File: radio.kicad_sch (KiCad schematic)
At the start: 17 parts, among them U18 RP2350B, U19 ABM8-272-T3_C20625731, U20 CC1101RGPR, U21 PE4259-63, U22 PN7150B0HN/C11002Y, U23 EM4095HMSO16B+, Y1 Crystal, Y3 Crystal

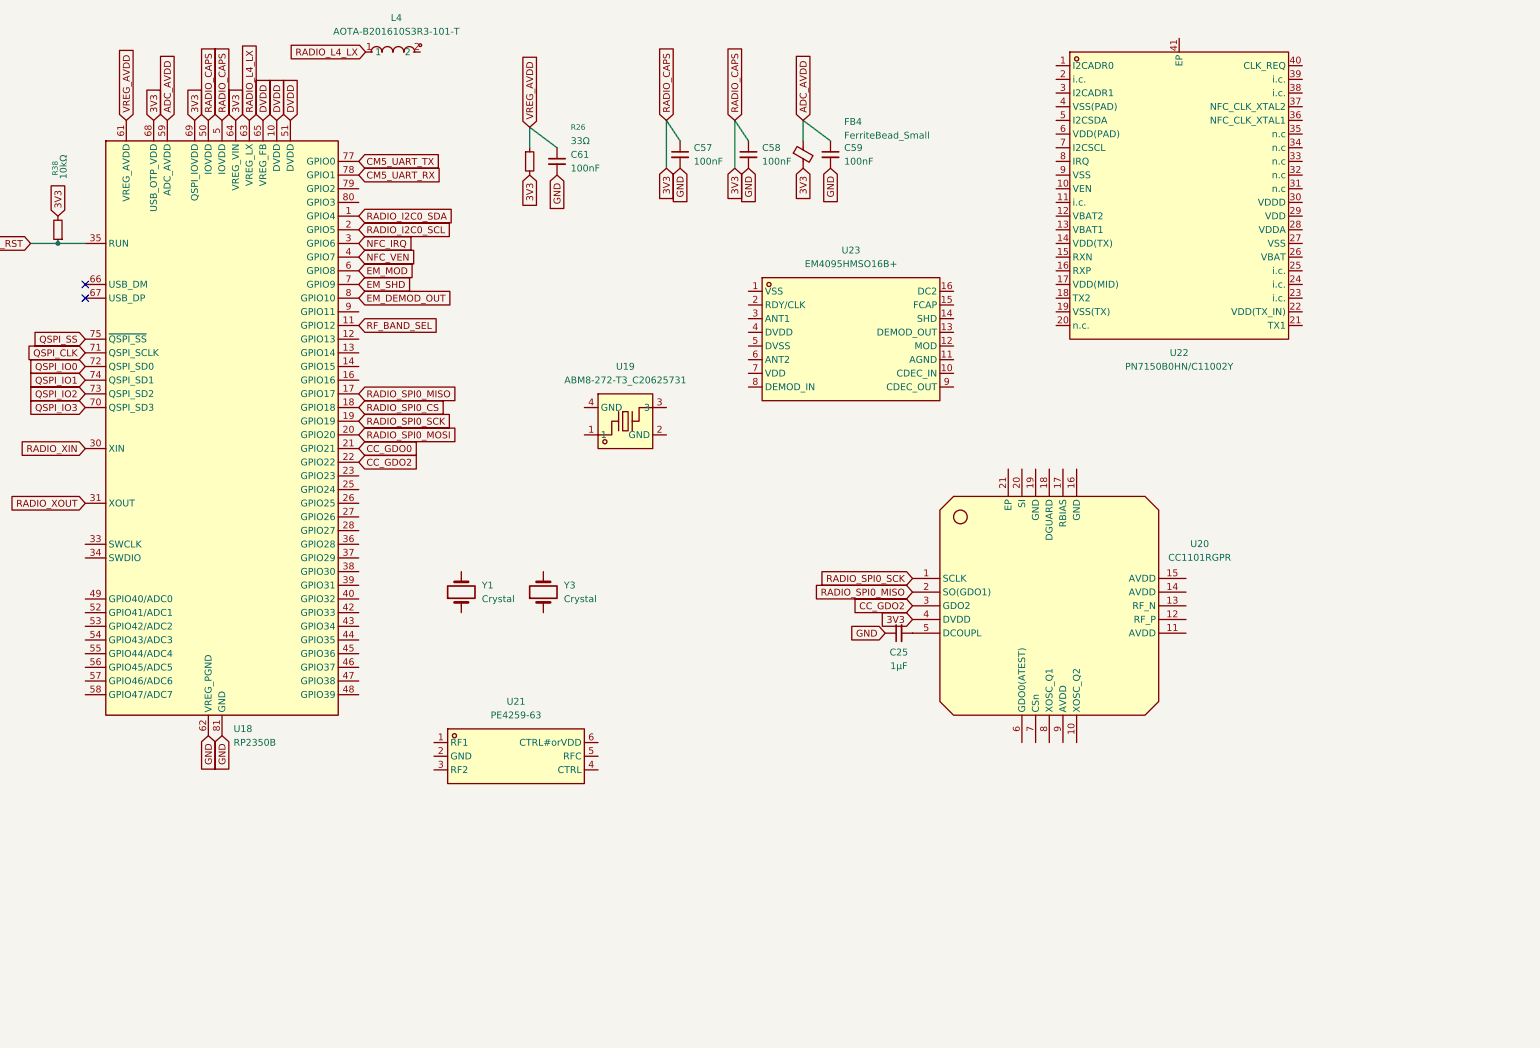
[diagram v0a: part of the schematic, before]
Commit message: finished cc1101 wiring, switched to single balun approach for dual sub-ghz bands, added sma port and footprints
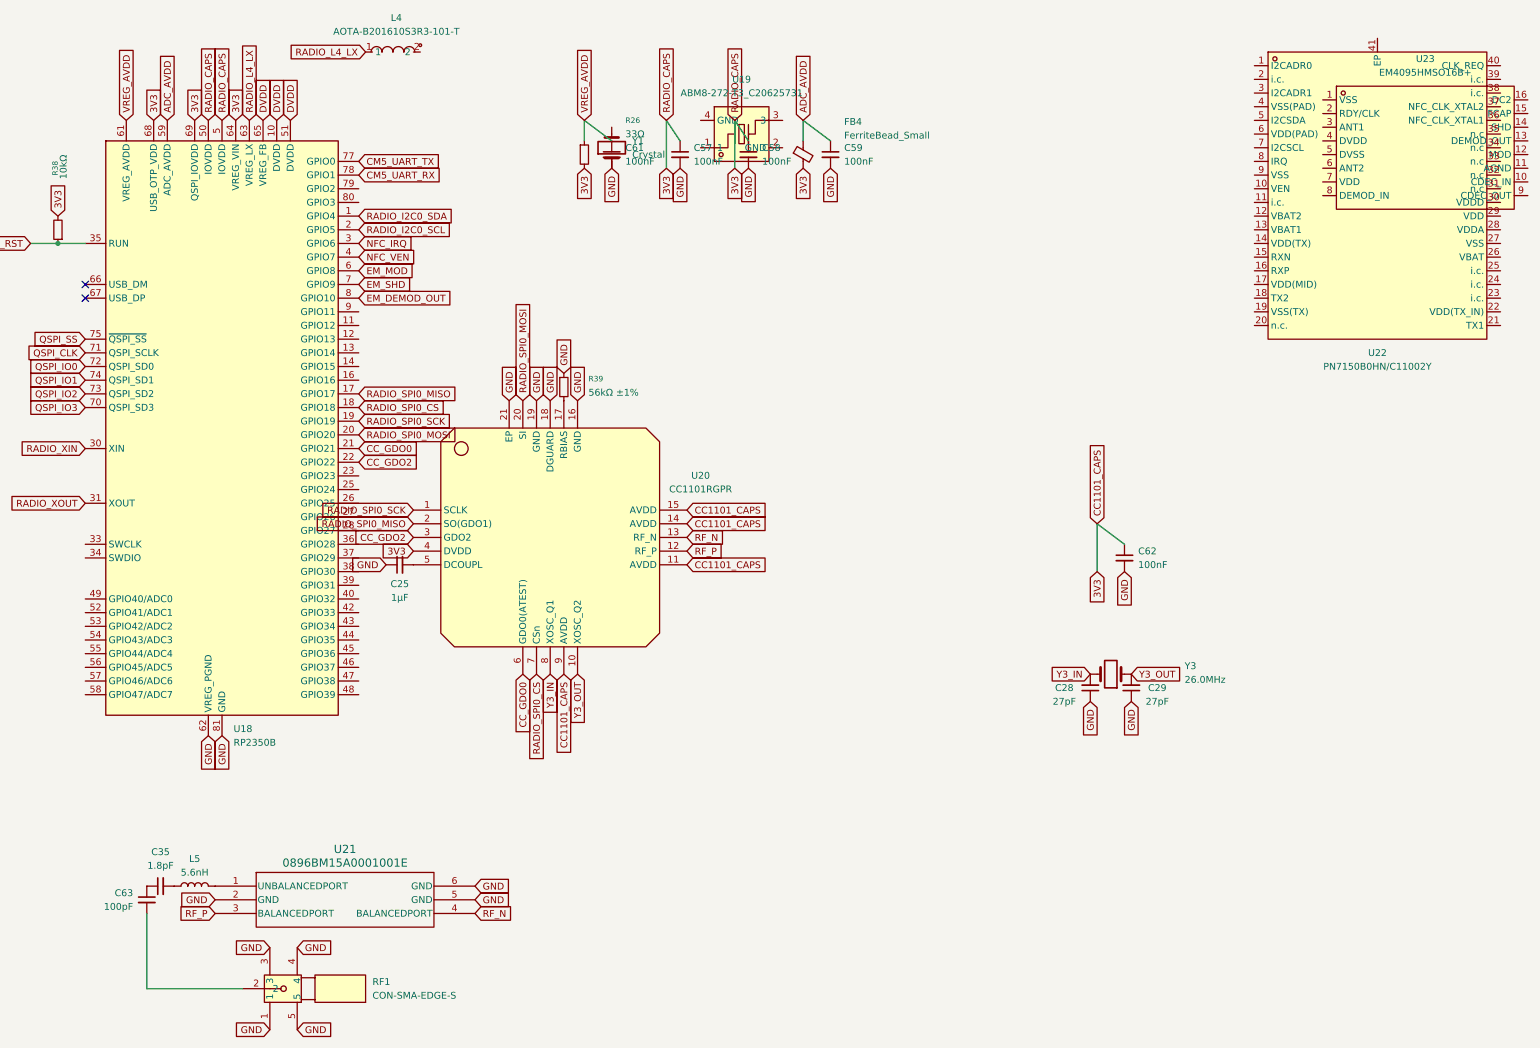
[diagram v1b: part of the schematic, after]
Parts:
- removed U21: PE4259-63, slate113:SC-70-6_L2.2-W1.3-P0.65-LS2.1-BL, symbol slate113:PE4259-63
- added C28, C29: 27pF, symbol Device:C_Small
- added C35: 1.8pF, symbol Device:C_Small
- added C62: 100nF, symbol Device:C_Small
- added C63: 100pF, symbol Device:C_Small
- added L5: 5.6nH, symbol Device:L
- added R39: 56kΩ ±1%, symbol Device:R_Small
- added RF1: CON-SMA-EDGE-S, slate113:SMA-SMD_CON-SMA-EDGE-S, symbol slate113:CON-SMA-EDGE-S
- added U21: 0896BM15A0001001E, slate113:SMD6_0896BM15A0001001E_JOT, symbol slate113:0896BM15A0001001E
- Y3: value Crystal -> 26.0MHz
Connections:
- net 3V3: now also U20.11 (AVDD), U20.14 (AVDD), U20.15 (AVDD), U20.9 (AVDD), C62.1
- net CC_GDO0: now also U20.6 (GDO0(ATEST))
- net GND: now also U20.16 (GND), U20.18 (DGUARD), U20.19 (GND), U20.21 (EP), Y1.1, C28.1, C29.1, C62.2, R39.1, RF1.1, RF1.3, RF1.4, RF1.5, U21.2 (GND), U21.5 (GND), U21.6 (GND)
- net RADIO_SPI0_CS: now also U20.7 (CSn)
- net RADIO_SPI0_MOSI: now also U20.20 (SI)
- net Y3_OUT: now reaches Y3.1
- net Y3_OUT: now also U20.10 (XOSC_Q2), C29.2
- net Y3_IN: now reaches Y3.2
- net Y3_IN: now also U20.8 (XOSC_Q1), C28.2
- net RF_P: now reaches U20.12 (RF_P)
- net RF_P: now also U21.3 (BALANCEDPORT)
- net RF_N: now reaches U20.13 (RF_N)
- net RF_N: now also U21.4 (BALANCEDPORT)
- net at U20.17 (RBIAS): now also R39.2
- net RF_BAND_SEL: no longer names the net of U18.11 (GPIO12)
- new net: C35.1, C63.1
- new net: C35.2, L5.1
- new net: C63.2, RF1.2
- new net: L5.2, U21.1 (UNBALANCEDPORT)
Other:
- moved on the sheet: C25, C61, R26, U19, U20, U22, U23, Y1, Y3

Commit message: worked on sub-ghz band switching with dual baluns and lc tuning, added second usb-c port, started nfc wiring, added switch footprint
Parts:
- added C60: 1.8pF, symbol Device:C_Small
- added C64, C65: 6.8pF, symbol Device:C_Small
- added C66: 20pF, symbol Device:C_Small
- added C67, C69, C70, C71: 100nF, symbol Device:C_Small
- added C68: 4.7µF, symbol Device:C_Small
- added FB5: FerriteBead, symbol Device:FerriteBead
- added L6, L7: 33nH, symbol Device:L
- added R40, R41: 5.1kΩ, symbol Device:R_Small
- added SW3: 4*4*1.7, slate113:SW-SMD_4P-L5.2-W5.2-P3.70-LS6.5, symbol slate113:4*4*1.7
- added U24, U25, U26, U27: PE4259-63, slate113:SC-70-6_L2.2-W1.3-P0.65-LS2.1-BL, symbol slate113:PE4259-63
- added U28: 0433BM15A0001001E, slate113:SMD6_0896BM15A0001001E_JOT, symbol slate113:0896BM15A0001001E
- added USB2: TYPE-C16PIN, slate113:USB-C-SMD_TYPE-C16PIN, symbol slate113:TYPE-C16PIN
- C35: value 1.8pF -> 20pF
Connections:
- net 3V3: now also U22.12 (VBAT2), U22.13 (VBAT1), U22.26 (VBAT), U22.6 (VDD(PAD)), C67.2, C68.1, C70.2, C71.2, U24.6 (CTRL#orVDD), U25.6 (CTRL#orVDD), U26.6 (CTRL#orVDD), U27.6 (CTRL#orVDD)
- net GND: now also C35.1, U19.2 (GND), U19.4 (GND), U22.1 (I2CADR0), U22.14 (VDD(TX)), U22.17 (VDD(MID)), U22.19 (VSS(TX)), U22.22 (VDD(TX_IN)), U22.27 (VSS), U22.28 (VDDA), U22.29 (VDD), U22.3 (I2CADR1), U22.30 (VDDD), U22.4 (VSS(PAD)), U22.41 (EP), U22.9 (VSS), C66.2, C67.1, C69.2, C70.1, C71.1, FB5.2, L6.2, L7.2, R40.2, R41.2, SW3.3, SW3.4, U24.2 (GND), U25.2 (GND), U26.2 (GND), U27.2 (GND), U28.2 (GND), U28.5 (GND), U28.6 (GND), USB2.A1B12 (GND), USB2.B1A12 (GND); no longer C61.2
- net NFC_IRQ: now also U22.8 (IRQ)
- net NFC_VEN: now also U22.10 (VEN)
- net QSPI_SS: now also SW3.1, SW3.2
- net RADIO_I2C0_SCL: now also U22.7 (I2CSCL)
- net RADIO_I2C0_SDA: now also U22.5 (I2CSDA)
- net RF_N: now also U27.5 (RFC); no longer U21.4 (BALANCEDPORT)
- net RF_P: now also U26.5 (RFC); no longer U21.3 (BALANCEDPORT)
- net 315MHZ_OUT: now reaches C63.1
- net 315MHZ_OUT: now also RF1.2, C65.2, U28.1 (UNBALANCEDPORT); no longer C35.1
- net at L5.1: now also C60.2; no longer C35.2
- net NFC_RX_N: now reaches U22.15 (RXN)
- net NFC_RX_P: now reaches U22.16 (RXP)
- net NFC_TX2: now reaches U22.18 (TX2)
- net NFC_TX1: now reaches U22.21 (TX1)
- net NFC_XTAL1: now reaches U22.36 (NFC_CLK_XTAL1)
- net NFC_XTAL1: now also U19.1, C66.1
- net NFC_XTAL2: now reaches U22.37 (NFC_CLK_XTAL2)
- net NFC_XTAL2: now also C35.2, U19.3
- net at Y1.2: now also C61.2
- net at C63.2: now also C60.1; no longer RF1.2
- net BAND_SEL_1: now reaches U18.11 (GPIO12)
- net BAND_SEL_1: now also U26.4 (CTRL), U27.4 (CTRL)
- net BAND_SEL_2: now reaches U18.12 (GPIO13)
- net BAND_SEL_2: now also U24.4 (CTRL), U25.4 (CTRL)
- new net: R40.1, USB2.A5 (CC1)
- new net: U25.5 (RFC), U27.3 (RF2)
- new net: R41.1, USB2.B5 (CC2)
- new net: U21.3 (BALANCEDPORT), U26.1 (RF1)
- new net: U24.5 (RFC), U26.3 (RF2)
- new net: C68.2, C69.1
- new net BADUSB_DM: USB2.A7 (DN1), USB2.B7 (DN2)
- new net BADUSB_DP: USB2.A6 (DP1), USB2.B6 (DP2)
- new net FerriteGND_RADIO: FB5.1, USB2.1 (SHELL), USB2.2 (SHELL), USB2.3 (SHELL), USB2.4 (SHELL)
- new net U21_BPN: U21.4 (BALANCEDPORT), U27.1 (RF1)
- new net U24_RF1: C64.1, C65.1, L7.1, U24.1 (RF1)
- new net U25_RF1: C64.2, L6.1, U25.1 (RF1)
- new net U28_BPN: U25.3 (RF2), U28.4 (BALANCEDPORT)
- new net U28_BPP: U24.3 (RF2), U28.3 (BALANCEDPORT)
- no-connect marks 2 -> 20
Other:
- note added: "3-Way SMA"
- note added: "315MHz Makeshift Balun"
- note added: "BOOTSEL Button"
- note added: "BadUSB Port"
- note added: "Band Filter"
- note added: "CC1101"
- note added: "Decoupling"
- note added: "Decoupling - 3V3"
- note added: "Misc"
- note added: "NFC"
- note added: "RP2350B"
- moved on the sheet: C25, C28, C29, C57, C58, C59, C61, C62, FB4, L4, R26, R38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

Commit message: switched nfc ic, wired rfid ic, blocked on coil parameters for radio schematic
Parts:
- removed U22: PN7150B0HN/C11002Y, slate113:VQFN-40_L6.0-W6.0-P0.50-TL-EP4.5, symbol slate113:PN7150B0HN_C11002Y
- added C72, C74, C75, C79: 2.2µF, symbol Device:C_Small
- added C73, C77: 100nF, symbol Device:C_Small
- added C76: 1µF, symbol Device:C_Small
- added C78: 160nF, symbol Device:C_Small
- added C80: 10nF, symbol Device:C_Small
- added C81: 6.8nF, symbol Device:C_Small
- added C82, C83, C84, C85: 4.7uF, symbol Device:C_Small
- added U29: PN7160A1HN/C100Y, slate113:HVQFN-40_L6.0-W6.0-P0.50-BL-EP4.1, symbol slate113:PN7160A1HN_C100Y
- C71: value 100nF -> 4.7µF
- U19: value ABM8-272-T3_C20625731 -> TXM27.12M0004322DBBDO00T
- Y1: value Crystal -> 12MHz
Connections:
- net 3V3: no longer C67.2, C68.1, C70.2, C71.2
- net BADUSB_DM: now also U18.66 (USB_DM)
- net BADUSB_DP: now also U18.67 (USB_DP)
- net DVDD: now also L4.2, C82.1, C83.1, C84.1, C85.1
- net EM_DEMOD_OUT: now also U23.13 (DEMOD_OUT)
- net EM_MOD: now also U23.12 (MOD)
- net EM_SHD: now also U23.14 (SHD)
- net GND: now also C68.1, C69.1, U23.1 (VSS), U23.5 (DVSS), C72.1, C73.1, C74.1, C75.1, C76.1, C78.1, C79.1, C80.1, C81.1, C82.2, C83.2, C84.2, C85.2, U29.1 (I2C_ADR0/SPI_NSS), U29.2 (DWL_REQ), U29.20 (VSS(TX)), U29.3 (l2C_ADR1/SPI_MOSI), U29.4 (Vss(PAD)), U29.41 (VSS), U29.9 (Vss(A)); no longer C67.1, C69.2, C70.1
- net NFC_IRQ: now also U29.8 (IRQ)
- net NFC_RX_N: now also U29.15 (RXN)
- net NFC_RX_P: now also U29.16 (RXP)
- net NFC_TX1: now also U29.21 (TX1)
- net NFC_TX2: now also U29.19 (TX2)
- net NFC_VEN: now also U29.10 (VEN)
- net NFC_XTAL1: now also U29.29 (XTAL2)
- net NFC_XTAL2: now also U29.30 (NFC_CLK_XTAL1)
- net RADIO_I2C0_SCL: now also U29.7 (I2C_SCL/SPI_SCK)
- net RADIO_I2C0_SDA: now also U29.5 (I2C_SDA/SPI_MISO)
- net NFC_VBAT: now reaches C68.2
- net NFC_VBAT: now also C69.2, C71.2, U29.12 (VBAT2), U29.13 (VDD(UP)), U29.28 (VBAT); no longer C69.1
- net at U23.10 (CDEC_IN): now also C77.2
- net at U23.11 (AGND): now also C78.2
- net at U23.15 (FCAP): now also C80.2
- net at U23.16 (DC2): now also C81.2
- net EM_RDY_CLK: now reaches U23.2 (RDY/CLK)
- net EM_RDY_CLK: now also U18.13 (GPIO14)
- net at U23.4 (DVDD): now also C67.2
- net at U23.7 (VDD): now also C70.2
- net at U23.9 (CDEC_OUT): now also C77.1
- new net 5V: C67.1, C70.1
- new net NFC_VDDCORE: C75.2, C79.2, U29.26 (VDD(A)), U29.27 (VDD), U29.31 (VDD(D))
- new net NFC_VDDPAD: C76.2, U29.6 (VDD(PAD))
- new net NFC_VDDTX: C72.2, C74.2, U29.14 (VDD(TX)), U29.18 (TVDD_IN), U29.22 (VDD_IN2)
- new net NFC_VMID: C73.2, U29.17 (VDD(VMID))
- no-connect marks 20 -> 17
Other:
- note added: "RFID"
- note removed: "Decoupling - 3V3"
- moved on the sheet: L4, U23

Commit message: finished gps schematic, updated footprints and 3d models
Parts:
- added C86: 100pF, symbol Device:C_Small
- added C87, C88: 33pF, symbol Device:C_Small
- added C89: 10µF, symbol Device:C_Small
- added C90, C92, C94: 100nF, symbol Device:C_Small
- added C91: 4.7µF, symbol Device:C_Small
- added C93: 2.2µF, symbol Device:C_Small
- added D2, D4: TVS, symbol Device:D
- added D3: TVS <0.6pF, symbol Device:D
- added L8: 68nH, symbol Device:L
- added Q1: NPN, symbol Simulation_SPICE:NPN
- added R42: 4.7kΩ, symbol Device:R_Small
- added R43: 10Ω, symbol Device:R_Small
- added R44: 47kΩ, symbol Device:R_Small
- added RF2: CON-SMA-EDGE-S, slate113:SMA-SMD_CON-SMA-EDGE-S, symbol slate113:CON-SMA-EDGE-S
- added U22: (no value), symbol slate113:LC29HCAMD
- added U30: SiP32508DT, Package_TO_SOT_SMD:TSOT-23-6, symbol Power_Management:SiP32508DT
- added U31, U32: S2B-PH-K-S-GW, slate113:CONN-TH_S2B-PH-K-S-GW, symbol slate113:S2B-PH-K-S-GW
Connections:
- net 3V3: now also C88.1, C91.1, C92.1, C93.1, D4.2 (A), U22.22 (V_BCKP)
- net GND: now also C87.2, C88.2, C89.2, C90.2, C91.2, C92.2, D2.1 (K), D3.1 (K), D4.1 (K), Q1.3 (E), RF2.1, RF2.3, RF2.4, RF2.5, U22.10 (GND), U22.12 (GND), U22.13 (GND), U22.24 (GND), U22.5 (D_SEL1), U22.6 (D_SEL2), U30.4 (GND)
- net RFID_ANT1: now reaches U23.3 (ANT1)
- net RFID_ANT1: now also U32.1
- net RFID_ANT2: now reaches U23.6 (ANT2)
- net RFID_ANT2: now also U32.2
- net NFC_ANT1: now reaches U29.23 (ANT1)
- net NFC_ANT1: now also U31.1
- net NFC_ANT2: now reaches U29.24 (ANT2)
- net NFC_ANT2: now also U31.2
- net GPS_1PPS: now reaches U18.14 (GPIO15)
- net GPS_1PPS: now also U22.3 (1PPS)
- net GPS_RESET: now reaches U18.16 (GPIO16)
- net GPS_RESET: now also R44.1
- net GPS_UART_TX: now reaches U18.25 (GPIO24)
- net GPS_UART_TX: now also U22.20 (TXD1/SPI_MISO)
- net GPS_UART_RX: now reaches U18.26 (GPIO25)
- net GPS_UART_RX: now also U22.21 (RXD1/SPI_MOSI)
- net GPS_EN: now reaches U18.79 (GPIO2)
- net GPS_EN: now also U30.3 (EN)
- net GPS_WI: now reaches U18.80 (GPIO3)
- net GPS_WI: now also U22.17 (WI)
- net GPS_WAKEUP: now reaches U18.9 (GPIO11)
- net GPS_WAKEUP: now also U22.1 (WAKEUP)
- new net: L8.1, R43.2
- new net: C94.2, U30.1 (OUT), U30.2 (OUT)
- new net: C93.2, U30.5 (IN), U30.6 (IN)
- new net GPS_3V3: C87.1, C89.1, C90.1, C94.1, D2.2 (A), R42.1, U22.23 (VCC)
- new net GPS_ANT: C86.1, D3.2 (A), L8.2, RF2.2
- new net GPS_RESET_N: Q1.1 (C), R42.2, U22.8 (RESET_N)
- new net GPS_RF_IN: C86.2, U22.11 (RF_IN)
- new net GPS_VDD_RF: R43.1, U22.9 (VDD_RF)
- new net NPN_B: Q1.2 (B), R44.2
- no-connect marks 17 -> 24
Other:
- note added: "Controller"
- note added: "GPS Power"

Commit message: finished radio board with load switches and flash, fixed b2b connector, started antenna module and rf sense switching circuit
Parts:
- removed C93: 2.2µF, symbol Device:C_Small
- removed C94: 100nF, symbol Device:C_Small
- removed RF1, RF2: CON-SMA-EDGE-S, slate113:SMA-SMD_CON-SMA-EDGE-S, symbol slate113:CON-SMA-EDGE-S
- removed U30: SiP32508DT, Package_TO_SOT_SMD:TSOT-23-6, symbol Power_Management:SiP32508DT
- added C95, C97: 2.2µF, symbol Device:C_Small
- added C96, C98: 100nF, symbol Device:C_Small
- added CN15: DF40C-20DP-0.4V, slate113:CONN-SMD_20P-P0.40_HRS_DF40TC-20DP-0.4V, symbol slate113:DF40C-20DP-0.4V
- added J19: SUBGHZ SMA, symbol Connector:Conn_Coaxial_Small
- added J20: GPS SMA, symbol Connector:Conn_Coaxial_Small
- added U33: W25Q128JVSIQTR, slate113:SOIC-8_L5.3-W5.3-P1.27-LS8.0-BL, symbol slate113:W25Q128JVSIQTR
- added U34, U35: SiP32508DT, Package_TO_SOT_SMD:TSOT-23-6, symbol Power_Management:SiP32508DT
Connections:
- net NFC_VBAT is gone; now on net GPS_VCC: C68.2, C69.2, C71.2, U29.12 (VBAT2), U29.13 (VDD(UP)), U29.28 (VBAT)
- net NFC_VDDPAD is gone; now on net GPS_VCC: C76.2, U29.6 (VDD(PAD))
- net 315MHZ_OUT: now also J19.1 (In)
- net 3V3: now also C95.1, CN15.7, U33.8 (VCC); no longer U20.4 (DVDD), U24.6 (CTRL#orVDD), U25.6 (CTRL#orVDD), U26.6 (CTRL#orVDD), U27.6 (CTRL#orVDD)
- net 5V: now also C97.1, CN15.9; no longer C67.1, C70.1
- net CM5_UART_RX: now also CN15.4
- net CM5_UART_TX: now also CN15.2
- net FerriteGND_RADIO: now also CN15.21, CN15.22, CN15.23, CN15.24
- net GND: now also CN15.1, CN15.10, CN15.11, CN15.12, CN15.3, CN15.5, J19.2 (Ext), J20.2 (Ext), U33.4 (GND), U34.4 (GND), U35.4 (GND)
- net GPS_ANT: now also J20.1 (In)
- net QSPI_CLK: now also U33.6 (CLK)
- net QSPI_IO0: now also U33.5 (DI)
- net QSPI_IO1: now also U33.2 (DO)
- net QSPI_IO2: now also U33.3 (IO2)
- net QSPI_IO3: now also U33.7 (IO3)
- net QSPI_SS: now also U33.1 (~{CS})
- net RP_RST: now also CN15.6
- net GPS_3V3 renamed GPS_VCC
- net GPS_VCC: now also U20.4 (DVDD), U24.6 (CTRL#orVDD), U25.6 (CTRL#orVDD), U26.6 (CTRL#orVDD), U27.6 (CTRL#orVDD), C96.1
- new net: C96.2, U34.1 (OUT), U34.2 (OUT)
- new net: C95.2, U34.5 (IN), U34.6 (IN)
- new net: C98.2, U35.1 (OUT), U35.2 (OUT)
- new net: C97.2, U35.5 (IN), U35.6 (IN)
- new net RADIO_5V: C67.1, C70.1, C98.1
- new net RADIO_EN: CN15.8, U34.3 (EN), U35.3 (EN)
- no-connect marks 24 -> 59
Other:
- note added: "Flash Chip | 16MB"
- note added: "Radio > Main"
- note added: "Radio Power"
- note removed: "GPS Power"
- moved on the sheet: C25, R39, U20
